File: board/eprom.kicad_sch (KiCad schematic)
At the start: 30 parts, among them J2 Conn_02x21_Counter_Clockwise, U3 TXB0108PW, U4 TXB0108PW, U5 TXB0108PW, U6 TXB0108PW, U7 TXB0108PW

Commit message: initial board layout (WIP), schematic tuning
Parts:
- C10, C11, C12, C13, C14, C15, C5, C6, C7, C8, C9: LCSC C115671 -> C307331
- C20: LCSC C274416 -> C23733
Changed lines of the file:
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@@
       (effects (font (size 1.27 1.27)) hide)
     )
-    (property "LCSC" "C115671" (at 220.98 78.74 0)
-      (effects (font (size 1.27 1.27)) hide)
-    )
-    (pin "2")
-    (pin "1")
+    (property "LCSC" "C307331" (at 220.98 78.74 0)
+      (effects (font (size 1.27 1.27)) hide)
+    )
+    (pin "1")
+    (pin "2")
     (instances
       (project "eprom5vread"
@@
       (effects (font (size 1.27 1.27)) hide)
     )
-    (property "LCSC" "C115671" (at 200.66 78.74 0)
-      (effects (font (size 1.27 1.27)) hide)
-    )
-    (pin "2")
-    (pin "1")
+    (property "LCSC" "C307331" (at 200.66 78.74 0)
+      (effects (font (size 1.27 1.27)) hide)
+    )
+    (pin "1")
+    (pin "2")
     (instances
       (project "eprom5vread"
@@
       (effects (font (size 1.27 1.27)) hide)
     )
-    (property "LCSC" "C115671" (at 200.66 140.97 0)
-      (effects (font (size 1.27 1.27)) hide)
-    )
-    (pin "2")
-    (pin "1")
+    (property "LCSC" "C307331" (at 200.66 140.97 0)
+      (effects (font (size 1.27 1.27)) hide)
+    )
+    (pin "1")
+    (pin "2")
     (instances
       (project "eprom5vread"
@@
       (effects (font (size 1.27 1.27)) hide)
     )
-    (pin "2")
-    (pin "1")
+    (pin "1")
+    (pin "2")
     (instances
       (project "eprom5vread"
@@
       (effects (font (size 1.27 1.27)) hide)
     )
-    (property "LCSC" "C115671" (at 129.54 116.84 0)
-      (effects (font (size 1.27 1.27)) hide)
-    )
-    (pin "2")
-    (pin "1")
+    (property "LCSC" "C307331" (at 129.54 116.84 0)
+      (effects (font (size 1.27 1.27)) hide)
+    )
+    (pin "1")
+    (pin "2")
     (instances
       (project "eprom5vread"
@@
       (effects (font (size 1.27 1.27)) hide)
     )
-    (property "LCSC" "C115671" (at 34.29 148.59 0)
-      (effects (font (size 1.27 1.27)) hide)
-    )
-    (pin "2")
-    (pin "1")
+    (property "LCSC" "C307331" (at 34.29 148.59 0)
+      (effects (font (size 1.27 1.27)) hide)
+    )
+    (pin "1")
+    (pin "2")
     (instances
       (project "eprom5vread"
@@
       (effects (font (size 1.27 1.27)) hide)
     )
-    (pin "18")
+    (pin "1")
+    (pin "10")
+    (pin "11")
+    (pin "12")
     (pin "13")
-    (pin "2")
-    (pin "10")
-    (pin "19")
-    (pin "16")
-    (pin "4")
-    (pin "17")
-    (pin "5")
-    (pin "9")
-    (pin "1")
-    (pin "11")
-    (pin "3")
-    (pin "12")
     (pin "14")
     (pin "15")
+    (pin "16")
+    (pin "17")
+    (pin "18")
+    (pin "19")
+    (pin "2")
     (pin "20")
+    (pin "3")
+    (pin "4")
+    (pin "5")
+    (pin "6")
     (pin "7")
     (pin "8")
-    (pin "6")
+    (pin "9")
     (instances
       (project "eprom5vread"
@@
       (effects (font (size 1.27 1.27)) hide)
     )
-    (pin "18")
+    (pin "1")
+    (pin "10")
+    (pin "11")
+    (pin "12")
     (pin "13")
-    (pin "2")
-    (pin "10")
-    (pin "19")
-    (pin "16")
-    (pin "4")
-    (pin "17")
-    (pin "5")
-    (pin "9")
-    (pin "1")
-    (pin "11")
-    (pin "3")
-    (pin "12")
     (pin "14")
     (pin "15")
+    (pin "16")
+    (pin "17")
+    (pin "18")
+    (pin "19")
+    (pin "2")
     (pin "20")
+    (pin "3")
+    (pin "4")
+    (pin "5")
+    (pin "6")
     (pin "7")
     (pin "8")
-    (pin "6")
+    (pin "9")
     (instances
       (project "eprom5vread"
@@
       (effects (font (size 1.27 1.27)) hide)
     )
-    (pin "18")
+    (pin "1")
+    (pin "10")
+    (pin "11")
+    (pin "12")
     (pin "13")
-    (pin "2")
-    (pin "10")
-    (pin "19")
-    (pin "16")
-    (pin "4")
-    (pin "17")
-    (pin "5")
-    (pin "9")
-    (pin "1")
-    (pin "11")
-    (pin "3")
-    (pin "12")
     (pin "14")
     (pin "15")
+    (pin "16")
+    (pin "17")
+    (pin "18")
+    (pin "19")
+    (pin "2")
     (pin "20")
+    (pin "3")
+    (pin "4")
+    (pin "5")
+    (pin "6")
     (pin "7")
     (pin "8")
-    (pin "6")
+    (pin "9")
     (instances
       (project "eprom5vread"
@@
       (effects (font (size 1.27 1.27)) hide)
     )
-    (property "LCSC" "C274416" (at 129.54 132.08 0)
-      (effects (font (size 1.27 1.27)) hide)
-    )
-    (pin "2")
-    (pin "1")
+    (property "LCSC" "C23733" (at 129.54 132.08 0)
+      (effects (font (size 1.27 1.27)) hide)
+    )
+    (pin "1")
+    (pin "2")
     (instances
       (project "eprom5vread"
@@
       (effects (font (size 1.27 1.27)) hide)
     )
-    (property "LCSC" "C115671" (at 220.98 140.97 0)
-      (effects (font (size 1.27 1.27)) hide)
-    )
-    (pin "2")
-    (pin "1")
+    (property "LCSC" "C307331" (at 220.98 140.97 0)
+      (effects (font (size 1.27 1.27)) hide)
+    )
+    (pin "1")
+    (pin "2")
     (instances
       (project "eprom5vread"
@@
       (effects (font (size 1.27 1.27)) hide)
     )
-    (property "LCSC" "C115671" (at 54.61 87.63 0)
-      (effects (font (size 1.27 1.27)) hide)
-    )
-    (pin "2")
-    (pin "1")
+    (property "LCSC" "C307331" (at 54.61 87.63 0)
+      (effects (font (size 1.27 1.27)) hide)
+    )
+    (pin "1")
+    (pin "2")
     (instances
       (project "eprom5vread"
@@
       (effects (font (size 1.27 1.27)) hide)
     )
-    (property "LCSC" "C115671" (at 54.61 25.4 0)
-      (effects (font (size 1.27 1.27)) hide)
-    )
-    (pin "2")
-    (pin "1")
+    (property "LCSC" "C307331" (at 54.61 25.4 0)
+      (effects (font (size 1.27 1.27)) hide)
+    )
+    (pin "1")
+    (pin "2")
     (instances
       (project "eprom5vread"
@@
       (effects (font (size 1.27 1.27)) hide)
     )
-    (property "LCSC" "C115671" (at 34.29 87.63 0)
-      (effects (font (size 1.27 1.27)) hide)
-    )
-    (pin "2")
-    (pin "1")
+    (property "LCSC" "C307331" (at 34.29 87.63 0)
+      (effects (font (size 1.27 1.27)) hide)
+    )
+    (pin "1")
+    (pin "2")
     (instances
       (project "eprom5vread"
@@
       (effects (font (size 1.27 1.27)) hide)
     )
-    (property "LCSC" "C115671" (at 34.29 25.4 0)
-      (effects (font (size 1.27 1.27)) hide)
-    )
-    (pin "2")
-    (pin "1")
+    (property "LCSC" "C307331" (at 34.29 25.4 0)
+      (effects (font (size 1.27 1.27)) hide)
+    )
+    (pin "1")
+    (pin "2")
     (instances
       (project "eprom5vread"
@@
       (effects (font (size 1.27 1.27)) hide)
     )
-    (pin "18")
+    (pin "1")
+    (pin "10")
+    (pin "11")
+    (pin "12")
     (pin "13")
-    (pin "2")
-    (pin "10")
-    (pin "19")
-    (pin "16")
-    (pin "4")
-    (pin "17")
-    (pin "5")
-    (pin "9")
-    (pin "1")
-    (pin "11")
-    (pin "3")
-    (pin "12")
     (pin "14")
     (pin "15")
+    (pin "16")
+    (pin "17")
+    (pin "18")
+    (pin "19")
+    (pin "2")
     (pin "20")
+    (pin "3")
+    (pin "4")
+    (pin "5")
+    (pin "6")
     (pin "7")
     (pin "8")
-    (pin "6")
+    (pin "9")
     (instances
       (project "eprom5vread"
@@
       (effects (font (size 1.27 1.27)) hide)
     )
-    (property "LCSC" "C115671" (at 54.61 148.59 0)
-      (effects (font (size 1.27 1.27)) hide)
-    )
-    (pin "2")
-    (pin "1")
+    (property "LCSC" "C307331" (at 54.61 148.59 0)
+      (effects (font (size 1.27 1.27)) hide)
+    )
+    (pin "1")
+    (pin "2")
     (instances
       (project "eprom5vread"
@@
       (effects (font (size 1.27 1.27)) hide)
     )
-    (pin "18")
+    (pin "1")
+    (pin "10")
+    (pin "11")
+    (pin "12")
     (pin "13")
-    (pin "2")
-    (pin "10")
-    (pin "19")
-    (pin "16")
-    (pin "4")
-    (pin "17")
-    (pin "5")
-    (pin "9")
-    (pin "1")
-    (pin "11")
-    (pin "3")
-    (pin "12")
     (pin "14")
     (pin "15")
+    (pin "16")
+    (pin "17")
+    (pin "18")
+    (pin "19")
+    (pin "2")
     (pin "20")
+    (pin "3")
+    (pin "4")
+    (pin "5")
+    (pin "6")
     (pin "7")
     (pin "8")
-    (pin "6")
-    (instances
-      (project "eprom5vread"
+    (pin "9")
+    (instances
+      (project "eprom5vread"

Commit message: finish board design
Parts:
- renumbered C6 to C201, C7 to C202, C8 to C203, C9 to C204, C10 to C205, C11 to C206, C15 to C207, C14 to C208, C13 to C209, C12 to C210, C20 to C211, C5 to C212, J2 to J201, NT4 to NT201, NT9 to NT202, NT5 to NT203, NT10 to NT204, NT6 to NT205, NT11 to NT206, NT12 to NT207, NT8 to NT208, NT13 to NT209, NT7 to NT210, R1 to R201, U3 to U201, U4 to U202, U5 to U203, U6 to U204, U7 to U205
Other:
- moved on the sheet: C201, C202, C203, C204, C205, C206, C207, C208, C209, C210, C211, C212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

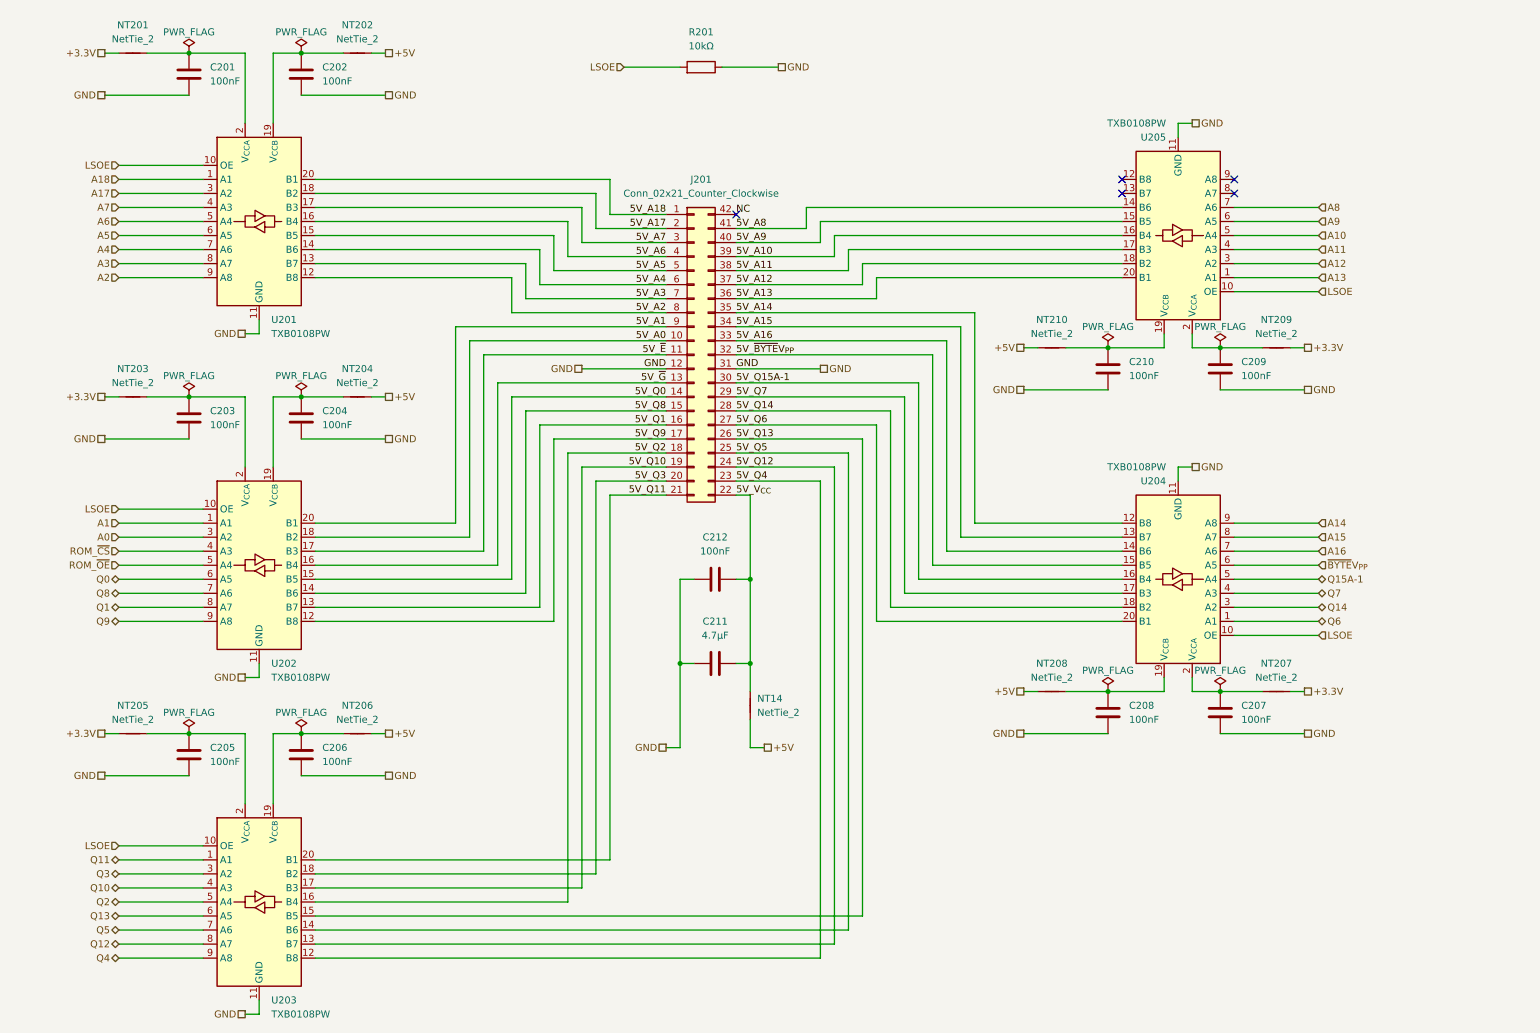
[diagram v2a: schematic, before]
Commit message: redo board to use I2C port expanders (and smaller MCU)
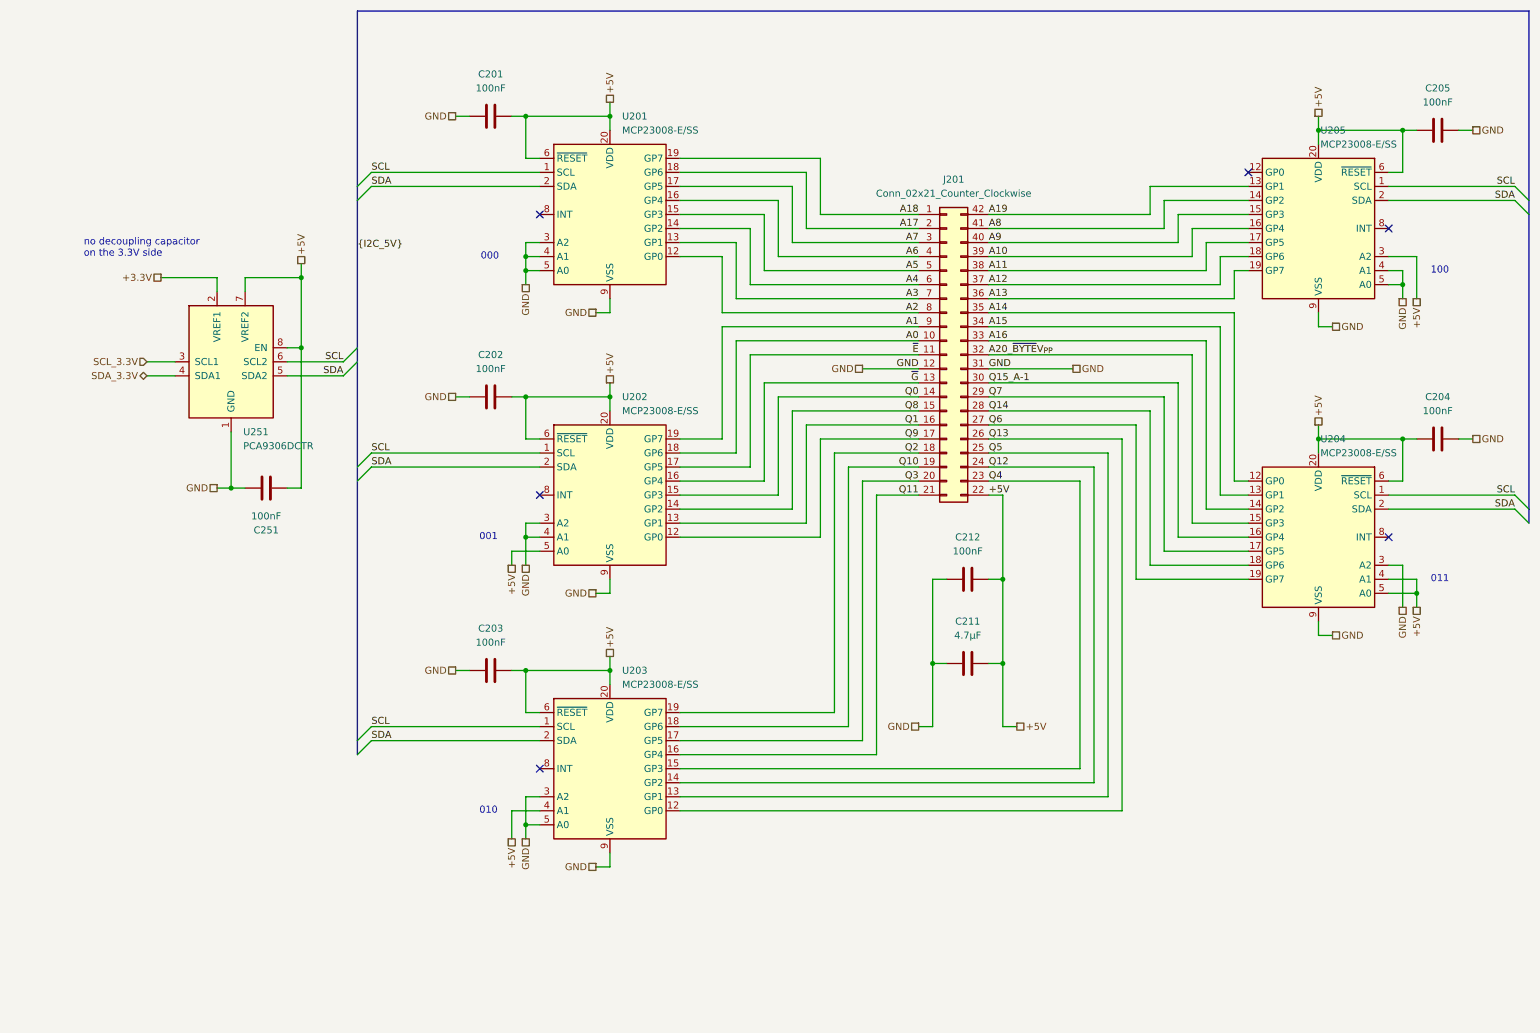
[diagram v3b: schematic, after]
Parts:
- removed C206, C207, C208, C209, C210: 100nF, Capacitor_SMD:C_0402_1005Metric, symbol Device:C
- removed NT14, NT201, NT202, NT203, NT204, NT205, NT206, NT207, NT208, NT209, NT210: NetTie_2, NetTie:NetTie-2_SMD_Pad0.5mm, symbol Device:NetTie_2
- removed R201: 10kΩ, Resistor_SMD:R_0402_1005Metric, symbol Device:R
- removed U201, U202, U203, U204, U205: TXB0108PW, Package_SO:TSSOP-20_4.4x6.5mm_P0.65mm, symbol Logic_LevelTranslator:TXB0108PW
- added C251: 100nF, Capacitor_SMD:C_0402_1005Metric, symbol Device:C
- added U201, U202, U203: MCP23008-E/SS, Package_SO:SSOP-20_5.3x7.2mm_P0.65mm, symbol Interface_Expansion_Inverted:MCP23008-xSS
- added U204, U205: MCP23008-E/SS, Package_SO:SSOP-20_5.3x7.2mm_P0.65mm, symbol Interface_Expansion:MCP23008-xSS
- added U251: PCA9306DCTR, Package_SO:SSOP-8_2.95x2.8mm_P0.65mm, symbol Interface:PCA9306
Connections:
- net 5V_A0 is gone; now on net A0: J201.10 (Pin_10)
- net 5V_A1 is gone; now on net A1: J201.9 (Pin_9)
- net 5V_A10 is gone; now on net A10: J201.39 (Pin_39)
- net 5V_A11 is gone; now on net A11: J201.38 (Pin_38)
- net 5V_A12 is gone; now on net A12: J201.37 (Pin_37)
- net 5V_A13 is gone; now on net A13: J201.36 (Pin_36)
- net 5V_A14 is gone; now on net A14: J201.35 (Pin_35)
- net 5V_A15 is gone; now on net A15: J201.34 (Pin_34)
- net 5V_A16 is gone; now on net A16: J201.33 (Pin_33)
- net 5V_A17 is gone; now on net A17: J201.2 (Pin_2)
- net 5V_A18 is gone; now on net A18: J201.1 (Pin_1)
- net 5V_A2 is gone; now on net A2: J201.8 (Pin_8)
- net 5V_A3 is gone; now on net A3: J201.7 (Pin_7)
- net 5V_A4 is gone; now on net A4: J201.6 (Pin_6)
- net 5V_A5 is gone; now on net A5: J201.5 (Pin_5)
- net 5V_A6 is gone; now on net A6: J201.4 (Pin_4)
- net 5V_A7 is gone; now on net A7: J201.3 (Pin_3)
- net 5V_A8 is gone; now on net A8: J201.41 (Pin_41)
- net 5V_A9 is gone; now on net A9: J201.40 (Pin_40)
- net 5V_Q0 is gone; now on net Q0: J201.14 (Pin_14)
- net 5V_Q1 is gone; now on net Q1: J201.16 (Pin_16)
- net 5V_Q10 is gone; now on net Q10: J201.19 (Pin_19)
- net 5V_Q11 is gone; now on net Q11: J201.21 (Pin_21)
- net 5V_Q12 is gone; now on net Q12: J201.24 (Pin_24)
- net 5V_Q13 is gone; now on net Q13: J201.26 (Pin_26)
- net 5V_Q14 is gone; now on net Q14: J201.28 (Pin_28)
- net 5V_Q2 is gone; now on net Q2: J201.18 (Pin_18)
- net 5V_Q3 is gone; now on net Q3: J201.20 (Pin_20)
- net 5V_Q4 is gone; now on net Q4: J201.23 (Pin_23)
- net 5V_Q5 is gone; now on net Q5: J201.25 (Pin_25)
- net 5V_Q6 is gone; now on net Q6: J201.27 (Pin_27)
- net 5V_Q7 is gone; now on net Q7: J201.29 (Pin_29)
- net 5V_Q8 is gone; now on net Q8: J201.15 (Pin_15)
- net 5V_Q9 is gone; now on net Q9: J201.17 (Pin_17)
- net 5V_V_{CC} is gone; now on net +5V: C211.2, C212.2, J201.22 (Pin_22)
- net +3.3V: now also U251.2 (VREF1)
- net +5V: now also C201.2, C202.2, C203.2, C204.2, C205.2, C251.2, U201.20 (VDD), U201.6 (~{RESET}), U202.20 (VDD), U202.5 (A0), U202.6 (~{RESET}), U203.20 (VDD), U203.4 (A1), U203.6 (~{RESET}), U204.20 (VDD), U204.4 (A1), U204.5 (A0), U204.6 (~{RESET}), U205.20 (VDD), U205.3 (A2), U205.6 (~{RESET}), U251.7 (VREF2), U251.8 (EN)
- net A0: now also U202.18 (GP6)
- net A1: now also U202.19 (GP7)
- net A10: now also U205.16 (GP4)
- net A11: now also U205.17 (GP5)
- net A12: now also U205.18 (GP6)
- net A13: now also U205.19 (GP7)
- net A14: now also U204.12 (GP0)
- net A15: now also U204.13 (GP1)
- net A16: now also U204.14 (GP2)
- net A17: now also U201.18 (GP6)
- net A18: now also U201.19 (GP7)
- net A2: now also U201.12 (GP0)
- net A3: now also U201.13 (GP1)
- net A4: now also U201.14 (GP2)
- net A5: now also U201.15 (GP3)
- net A6: now also U201.16 (GP4)
- net A7: now also U201.17 (GP5)
- net A8: now also U205.14 (GP2)
- net A9: now also U205.15 (GP3)
- net GND: now also C201.1, C202.1, C203.1, C204.1, C205.1, C251.1, U201.3 (A2), U201.4 (A1), U201.5 (A0), U201.9 (VSS), U202.3 (A2), U202.4 (A1), U202.9 (VSS), U203.3 (A2), U203.5 (A0), U203.9 (VSS), U204.3 (A2), U204.9 (VSS), U205.4 (A1), U205.5 (A0), U205.9 (VSS), U251.1 (GND); no longer C201.2, C202.2, C203.2, C204.2, C205.2
- net Q0: now also U202.15 (GP3)
- net Q1: now also U202.13 (GP1)
- net Q10: now also U203.18 (GP6)
- net Q11: now also U203.16 (GP4)
- net Q12: now also U203.14 (GP2)
- net Q13: now also U203.12 (GP0)
- net Q14: now also U204.18 (GP6)
- net Q2: now also U203.19 (GP7)
- net Q3: now also U203.17 (GP5)
- net Q4: now also U203.15 (GP3)
- net Q5: now also U203.13 (GP1)
- net Q6: now also U204.19 (GP7)
- net Q7: now also U204.17 (GP5)
- net Q8: now also U202.14 (GP2)
- net Q9: now also U202.12 (GP0)
- net 5V_Q15A-1 renamed Q15_A-1
- net Q15_A-1: now also U204.16 (GP4)
- net 5V_~{BYTE}V_{PP} renamed A20_~{BYTE}V_{PP}
- net A20_~{BYTE}V_{PP}: now also U204.15 (GP3)
- net 5V_~{E} renamed ~{E}
- net ~{E}: now also U202.17 (GP5)
- net 5V_~{G} renamed ~{G}
- net ~{G}: now also U202.16 (GP4)
- net NC renamed A19
- net A19: now also U205.13 (GP1)
- new net SCL: U201.1 (SCL), U202.1 (SCL), U203.1 (SCL), U204.1 (SCL), U205.1 (SCL), U251.6 (SCL2)
- new net SCL_3.3V: U251.3 (SCL1)
- new net SDA: U201.2 (SDA), U202.2 (SDA), U203.2 (SDA), U204.2 (SDA), U205.2 (SDA), U251.5 (SDA2)
- new net SDA_3.3V: U251.4 (SDA1)
- no-connect marks 5 -> 6
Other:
- note added: "000"
- note added: "001"
- note added: "010"
- note added: "011"
- note added: "100"
- note added: "no decoupling capacitor on the 3.3V side"
- moved on the sheet: C211, C212, J201
